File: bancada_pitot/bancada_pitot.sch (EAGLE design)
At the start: 18 parts

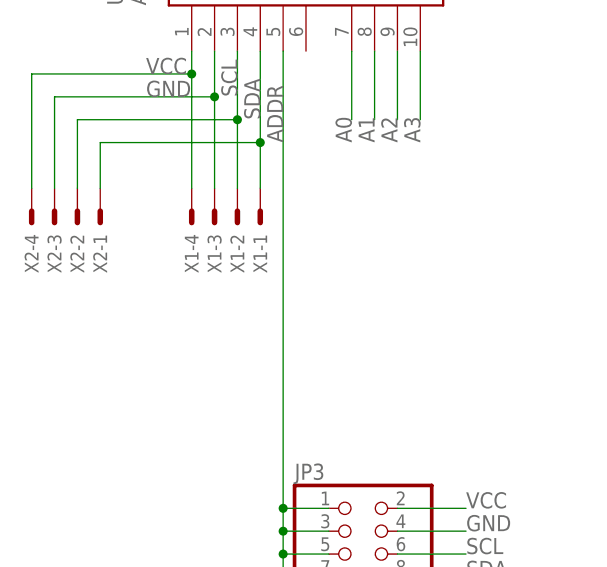
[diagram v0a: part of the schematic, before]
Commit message: KK connectors changed from 4mm to 2.54mm
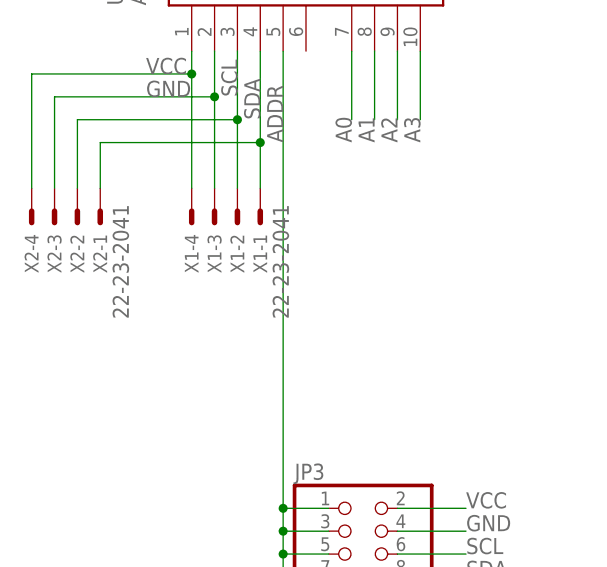
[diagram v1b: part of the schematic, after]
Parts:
- X1, X2: value (none) -> 22-23-2041; device con-molex:KK-156-4 -> con-molex:22-23-2041
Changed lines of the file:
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@@
 <part name="GND21" library="supply1" library_urn="urn:adsk.eagle:library:371" deviceset="GND" device=""/>
 <part name="U$1" library="diy_modules" deviceset="ADC-4CH-ADS1115" device=""/>
-<part name="X1" library="con-molex" library_urn="urn:adsk.eagle:library:165" deviceset="KK-156-4" device=""/>
-<part name="X2" library="con-molex" library_urn="urn:adsk.eagle:library:165" deviceset="KK-156-4" device=""/>
+<part name="X1" library="con-molex" library_urn="urn:adsk.eagle:library:165" deviceset="22-23-2041" device=""/>
+<part name="X2" library="con-molex" library_urn="urn:adsk.eagle:library:165" deviceset="22-23-2041" device=""/>
 <part name="JP3" library="pinhead" library_urn="urn:adsk.eagle:library:325" deviceset="PINHD-2X4" device="" package3d_urn="urn:adsk.eagle:package:22461/2"/>
 </parts>

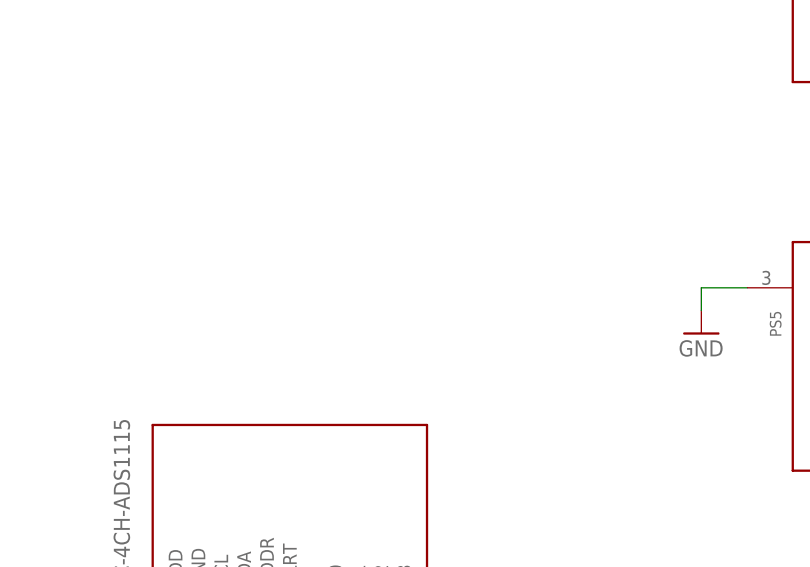
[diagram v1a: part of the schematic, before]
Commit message: Add jumpers (or 0ohm resistors)
In previous design, some ground planes were unconnected to each other. It was meant to be added jumper wires after production.

This commit changes this to actual jumpers, with pins, so they don't need to be soldered from bottom, but can actually be placed on top, like any other through-hole component. 0ohm through-hole resistors can also be used.
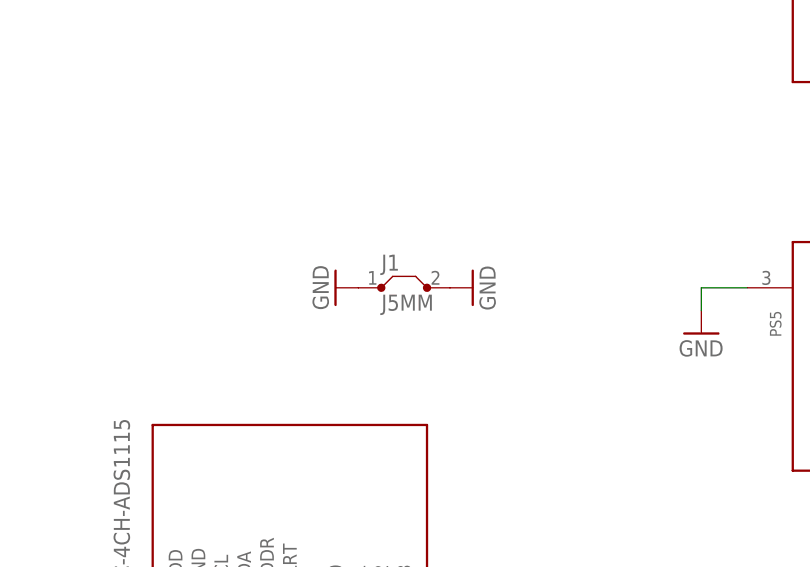
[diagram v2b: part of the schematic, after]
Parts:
- added J1: J5MM, jumper:J5MM
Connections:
- net GND: now also J1.1, J1.2
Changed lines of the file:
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@@
 <?xml version="1.0" encoding="utf-8"?>
 <!DOCTYPE eagle SYSTEM "eagle.dtd">
-<eagle version="8.6.0">
+<eagle version="9.0.0">
 <drawing>
 <settings>
@@
 <part name="X2" library="con-molex" library_urn="urn:adsk.eagle:library:165" deviceset="22-23-2041" device=""/>
 <part name="JP3" library="pinhead" library_urn="urn:adsk.eagle:library:325" deviceset="PINHD-2X4" device="" package3d_urn="urn:adsk.eagle:package:22461/2"/>
+<part name="J1" library="jumper" library_urn="urn:adsk.eagle:library:252" deviceset="J" device="5MM" package3d_urn="urn:adsk.eagle:package:15465/1"/>
+<part name="GND1" library="supply1" library_urn="urn:adsk.eagle:library:371" deviceset="GND" device=""/>
+<part name="GND2" library="supply1" library_urn="urn:adsk.eagle:library:371" deviceset="GND" device=""/>
 </parts>
 <sheets>
@@
 <instance part="X2" gate="-4" x="-20.32" y="142.24" rot="R270"/>
 <instance part="JP3" gate="A" x="15.24" y="104.14"/>
+<instance part="J1" gate="1" x="22.86" y="200.66"/>
+<instance part="GND1" gate="1" x="30.48" y="200.66" rot="R90"/>
+<instance part="GND2" gate="1" x="15.24" y="200.66" rot="R270"/>
 </instances>
 <busses>
@@
 <wire x1="20.32" y1="106.68" x2="27.94" y2="106.68" width="0.1524" layer="91"/>
 </segment>
+<segment>
+<pinref part="J1" gate="1" pin="2"/>
+<pinref part="GND1" gate="1" pin="GND"/>
+</segment>
+<segment>
+<pinref part="J1" gate="1" pin="1"/>
+<pinref part="GND2" gate="1" pin="GND"/>
+</segment>
 </net>
